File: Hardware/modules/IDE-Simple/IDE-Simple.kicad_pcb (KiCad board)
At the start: 4 copper layers, 83.3 x 68.2 mm, 13 parts, among them J1 Conn_02x20_Odd_Even, J2 Conn_02x22_Odd_Even, J3 Bus_PCI_6502, U1 74HC138, U2 74AHC2G00

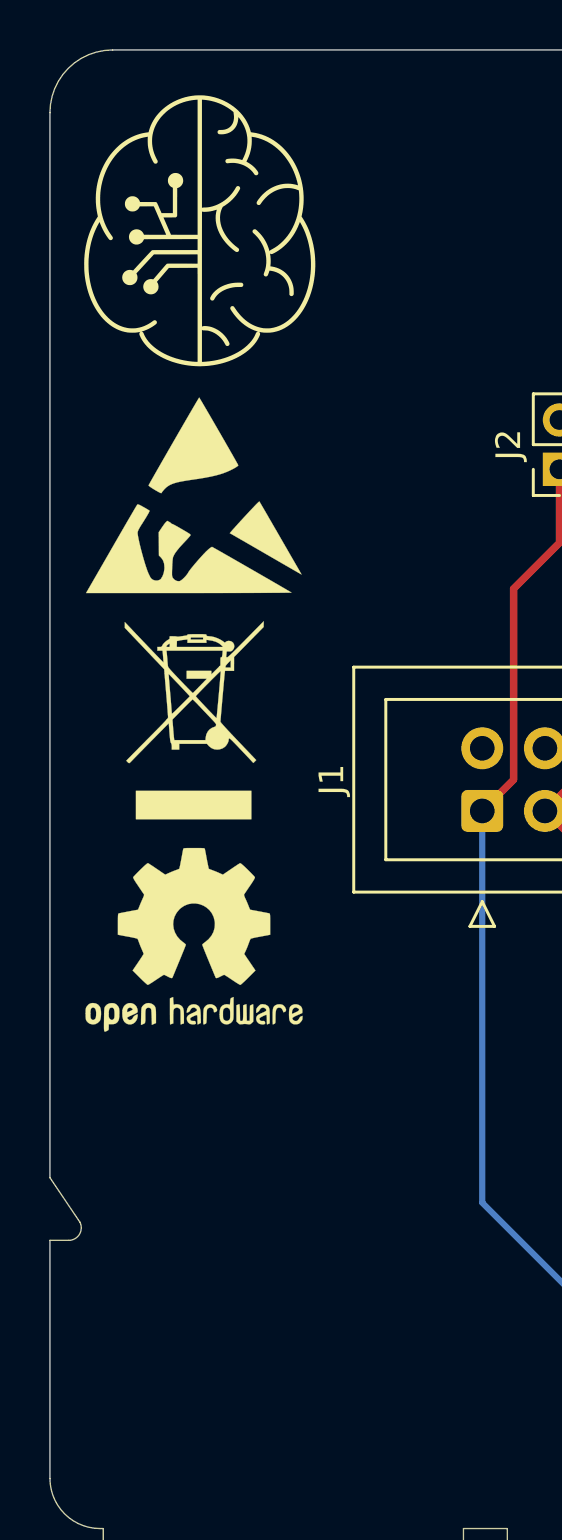
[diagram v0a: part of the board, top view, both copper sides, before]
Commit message: Hardware Update Add MyCPU VGA Module Beautify all Schematics minor Error corrections Readme Update
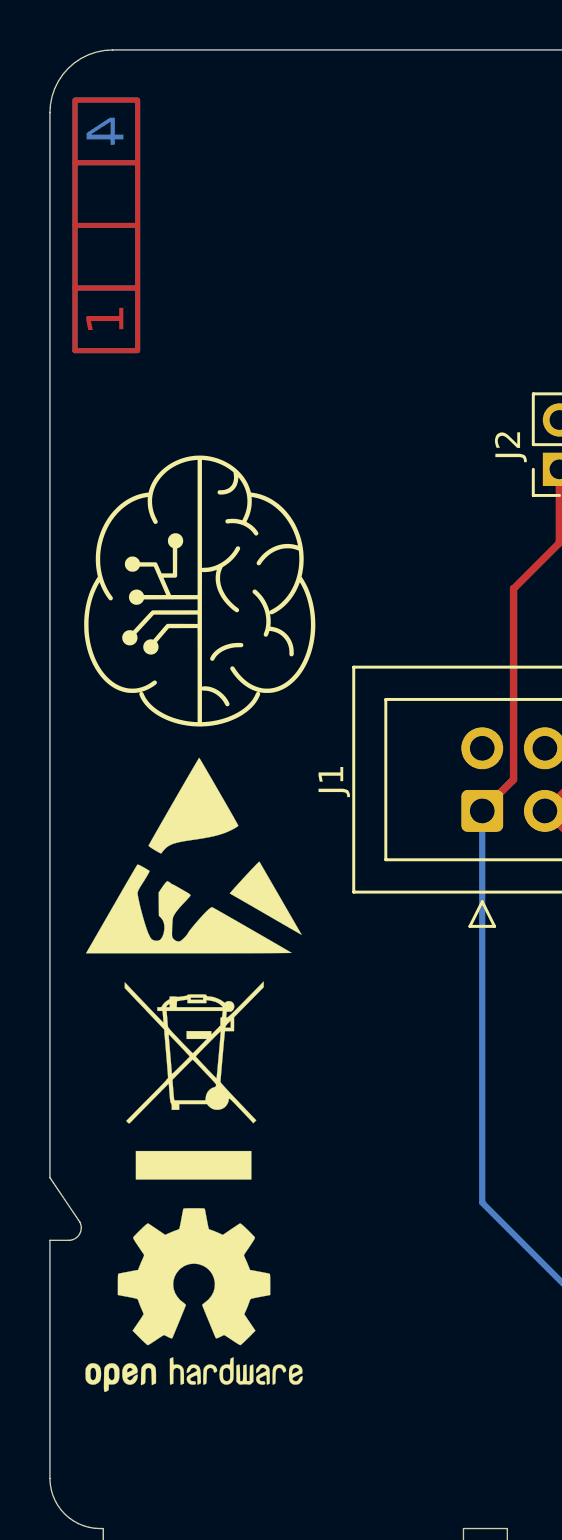
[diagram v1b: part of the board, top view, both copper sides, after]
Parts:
- added Ref**: Val**, Eigene:ladder_4, F.Cu at (114.4, 65.9)
- moved G*** 14.6 mm to (118.2, 80.8)
- moved REF** 14.6 mm to (118.0, 91.4)
- moved REF** 14.6 mm to (118.0, 109.5)
- moved REF** 14.6 mm to (118.0, 100.6)

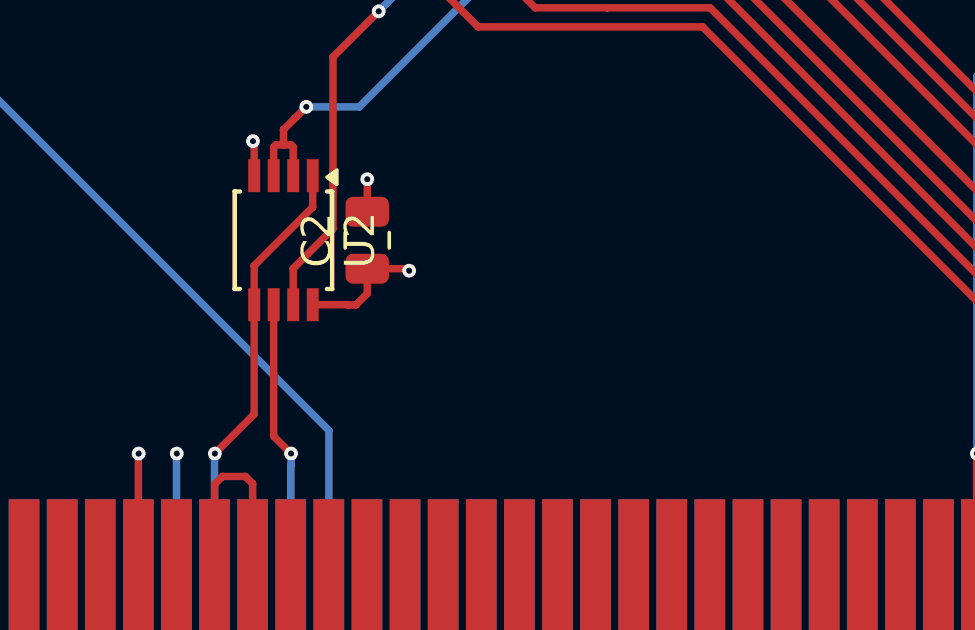
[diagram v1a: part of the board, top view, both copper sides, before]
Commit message: Hardware Review Pt. 1 fix Address Decoding for Strobe Generators add bulk capacitance to every board fix wiring of Prototyping Board
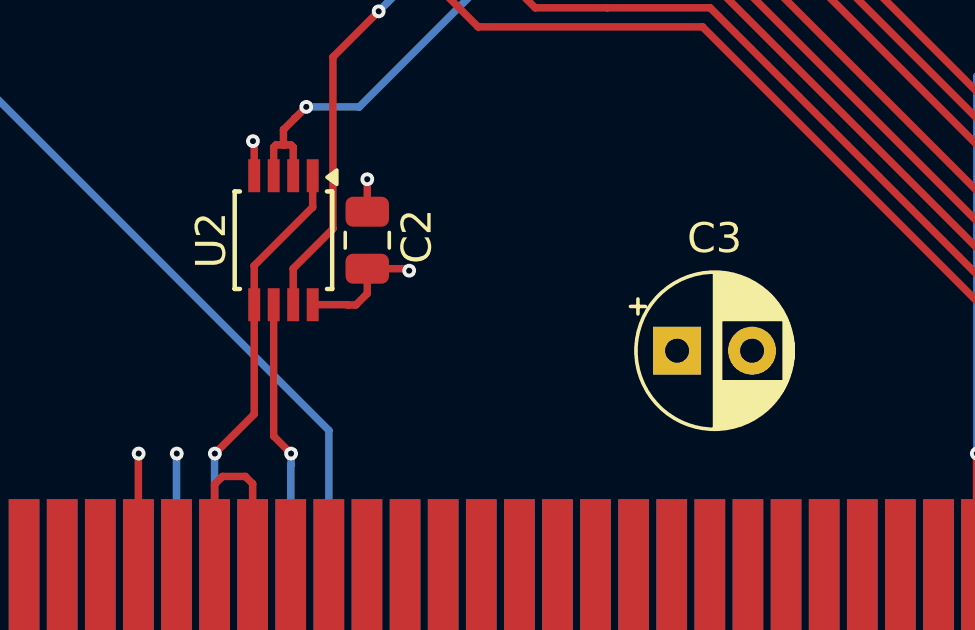
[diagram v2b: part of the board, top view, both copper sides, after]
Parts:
- added C3: 10µ, Capacitor_THT:CP_Radial_D5.0mm_P2.50mm, F.Cu at (153.5, 115.1)
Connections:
- D1 pad 1: Net-(D1-K) -> (no net)
- J1 pad 10: unconnected-(J1-Pin_10-Pad10) -> (no net)
- J1 pad 12: unconnected-(J1-Pin_12-Pad12) -> (no net)
- J1 pad 14: unconnected-(J1-Pin_14-Pad14) -> (no net)
- J1 pad 16: unconnected-(J1-Pin_16-Pad16) -> (no net)
- J1 pad 18: unconnected-(J1-Pin_18-Pad18) -> (no net)
- J1 pad 21: unconnected-(J1-Pin_21-Pad21) -> (no net)
- J1 pad 27: unconnected-(J1-Pin_27-Pad27) -> (no net)
- J1 pad 28: unconnected-(J1-Pin_28-Pad28) -> (no net)
- J1 pad 29: unconnected-(J1-Pin_29-Pad29) -> (no net)
- J1 pad 31: unconnected-(J1-Pin_31-Pad31) -> (no net)
- J1 pad 32: unconnected-(J1-Pin_32-Pad32) -> (no net)
- J1 pad 34: unconnected-(J1-Pin_34-Pad34) -> (no net)
- J1 pad 4: unconnected-(J1-Pin_4-Pad4) -> (no net)
- J1 pad 6: unconnected-(J1-Pin_6-Pad6) -> (no net)
- J1 pad 8: unconnected-(J1-Pin_8-Pad8) -> (no net)
- J2 pad 10: unconnected-(J2-Pin_10-Pad10) -> (no net)
- J2 pad 12: unconnected-(J2-Pin_12-Pad12) -> (no net)
- J2 pad 14: unconnected-(J2-Pin_14-Pad14) -> (no net)
- J2 pad 16: unconnected-(J2-Pin_16-Pad16) -> (no net)
- J2 pad 18: unconnected-(J2-Pin_18-Pad18) -> (no net)
- J2 pad 21: unconnected-(J2-Pin_21-Pad21) -> (no net)
- J2 pad 27: unconnected-(J2-Pin_27-Pad27) -> (no net)
- J2 pad 28: unconnected-(J2-Pin_28-Pad28) -> (no net)
- J2 pad 29: unconnected-(J2-Pin_29-Pad29) -> (no net)
- J2 pad 31: unconnected-(J2-Pin_31-Pad31) -> (no net)
- J2 pad 32: unconnected-(J2-Pin_32-Pad32) -> (no net)
- J2 pad 34: unconnected-(J2-Pin_34-Pad34) -> (no net)
- J2 pad 4: unconnected-(J2-Pin_4-Pad4) -> (no net)
- J2 pad 6: unconnected-(J2-Pin_6-Pad6) -> (no net)
- J2 pad 8: unconnected-(J2-Pin_8-Pad8) -> (no net)
- J3 pad A11: /A13 -> (no net)
- J3 pad A12: /A15 -> (no net)
- J3 pad A25: /~{ROM} -> (no net)
- J3 pad A27: /~{IRQ_0.0} -> (no net)
- J3 pad A28: /~{IRQ_0.1} -> (no net)
- J3 pad A29: /~{IRQ_0.2} -> (no net)
- J3 pad A30: /~{IRQ_0.3} -> (no net)
- J3 pad A31: /~{IRQ_0.4} -> (no net)
- J3 pad A32: /~{IRQ_0.5} -> (no net)
- J3 pad A33: /~{IRQ_0.6} -> (no net)
- J3 pad A34: /~{IRQ_0.7} -> (no net)
- J3 pad A38: /SYNC_VPA -> (no net)
- J3 pad A39: /Ø2/VDA -> (no net)
- J3 pad A41: /~{RDY} -> (no net)
- J3 pad A42: /~{BE} -> (no net)
- J3 pad A45: /E -> (no net)
- J3 pad A53: /RAM_0 -> (no net)
- J3 pad A54: /RAM_1 -> (no net)
- J3 pad A55: /RAM_2 -> (no net)
- J3 pad A56: /RAM_3 -> (no net)
- J3 pad A58: /RAM_4 -> (no net)
- J3 pad A59: /RAM_5 -> (no net)
- J3 pad A60: /RAM_6 -> (no net)
- J3 pad A61: /RAM_7 -> (no net)
- J3 pad A8: /A9 -> (no net)
- J3 pad A9: /A11 -> (no net)
- J3 pad B11: /A12 -> (no net)
- J3 pad B12: /A14 -> (no net)
- J3 pad B24: /~{L_RAM} -> (no net)
- J3 pad B25: /~{H_RAM} -> (no net)
- J3 pad B27: /~{IRQ} -> (no net)
- J3 pad B28: /~{IRQ_0} -> (no net)
- J3 pad B29: /~{IRQ_1} -> (no net)
- J3 pad B30: /~{IRQ_2} -> (no net)
- J3 pad B31: /~{IRQ_3} -> (no net)
- J3 pad B32: /~{IRQ_4} -> (no net)
- J3 pad B33: /~{NMI} -> (no net)
- J3 pad B34: /PAGE -> (no net)
- J3 pad B38: /~{VP} -> (no net)
- J3 pad B39: /~{ML} -> (no net)
- J3 pad B46: /M/X -> (no net)
- J3 pad B53: /ROM_0 -> (no net)
- J3 pad B54: /ROM_1 -> (no net)
- J3 pad B55: /ROM_2 -> (no net)
- J3 pad B56: /ROM_3 -> (no net)
- J3 pad B58: /ROM_4 -> (no net)
- J3 pad B59: /ROM_5 -> (no net)
- J3 pad B60: /ROM_6 -> (no net)
- J3 pad B61: /ROM_7 -> (no net)
- J3 pad B8: /A8 -> (no net)
- J3 pad B9: /A10 -> (no net)
- R1 pad 2: Net-(D1-K) -> (no net)
- U1 pad 10: unconnected-(U1-~{Y5}-Pad10) -> (no net)
- U1 pad 11: unconnected-(U1-~{Y4}-Pad11) -> (no net)
- U1 pad 12: unconnected-(U1-~{Y3}-Pad12) -> (no net)
- U1 pad 13: unconnected-(U1-~{Y2}-Pad13) -> (no net)
- U1 pad 14: unconnected-(U1-~{Y1}-Pad14) -> (no net)
- U1 pad 7: unconnected-(U1-~{Y7}-Pad7) -> (no net)
- U1 pad 9: unconnected-(U1-~{Y6}-Pad9) -> (no net)
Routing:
- net Net-(D1-K): track 1.58 -> 0.00 mm
- net (no net): track 0.00 -> 1.58 mm

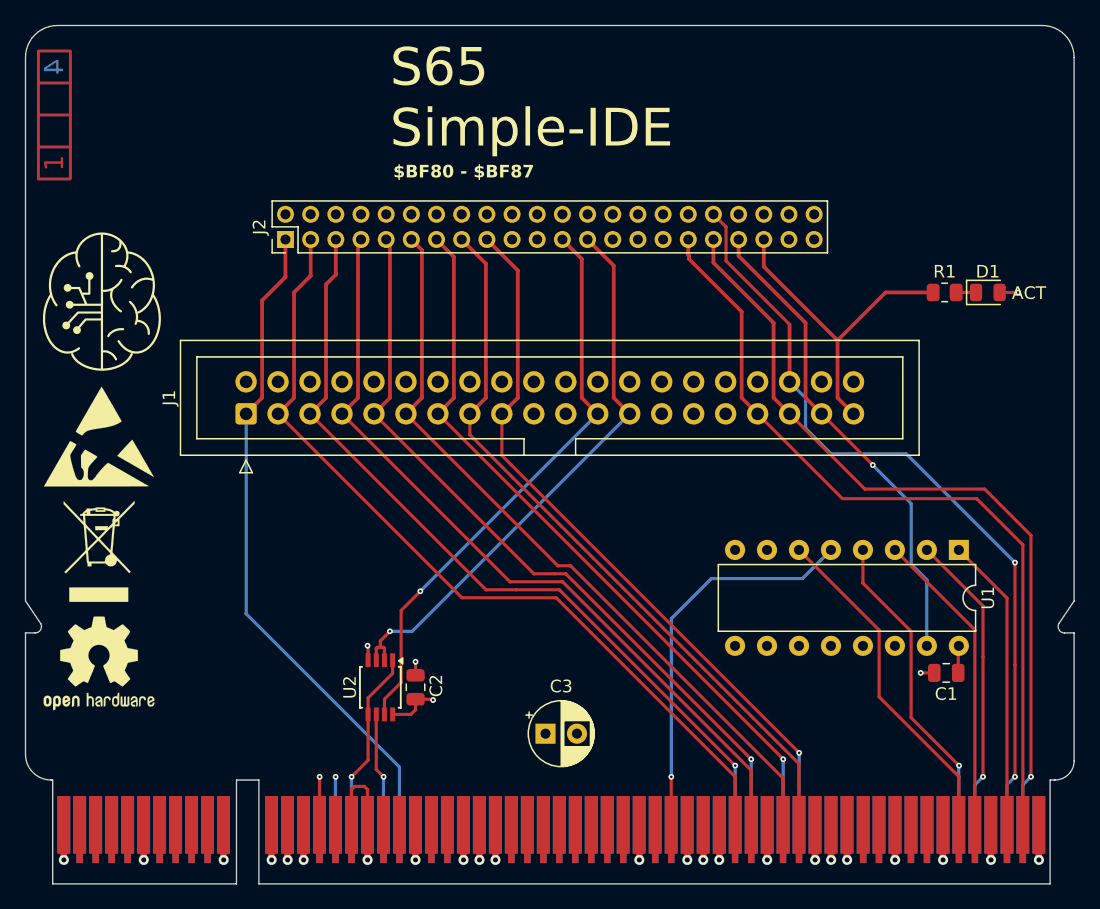
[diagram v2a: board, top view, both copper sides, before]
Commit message: Big Review Update - Changed Copper Pours on all PCBs - Implemented errors found at review - fixed some additional errors
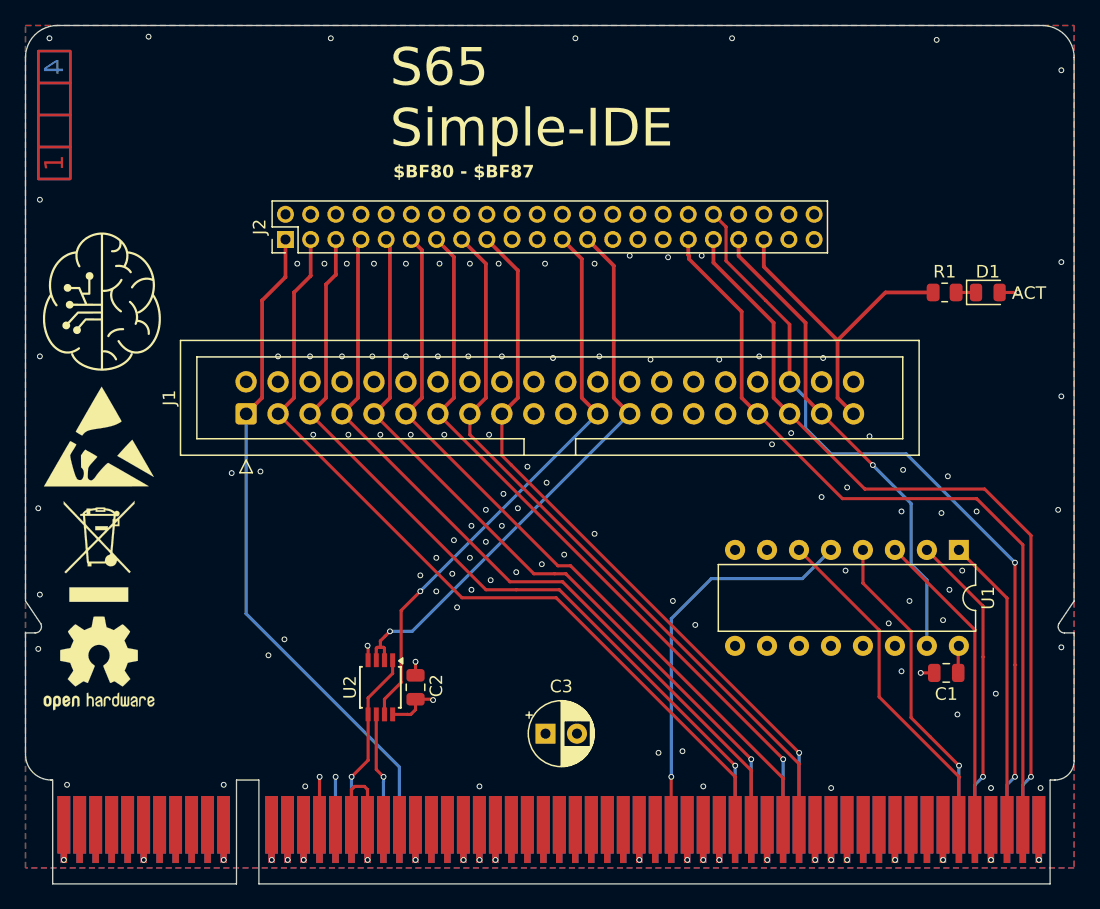
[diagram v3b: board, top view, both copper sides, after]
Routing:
- net +5V: vias 6 -> 111
- added copper zone on B.Cu, net +5V
- added copper zone on F.Cu, net +5V
- added copper zone on In1.Cu, net GND
- removed copper zone on In1.Cu, net +5V
